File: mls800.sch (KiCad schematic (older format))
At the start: 43 parts, among them CON1 BARREL_JACK, IC1 6N137, J1 USB, P1 CONN_02X03, P2 DIN_5, P3 DIN_5, P4 CONN_02X03, P5 CONN_02X03, SW1 SW_TACT_LED, U1 LM340MP-5.0/NOPB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

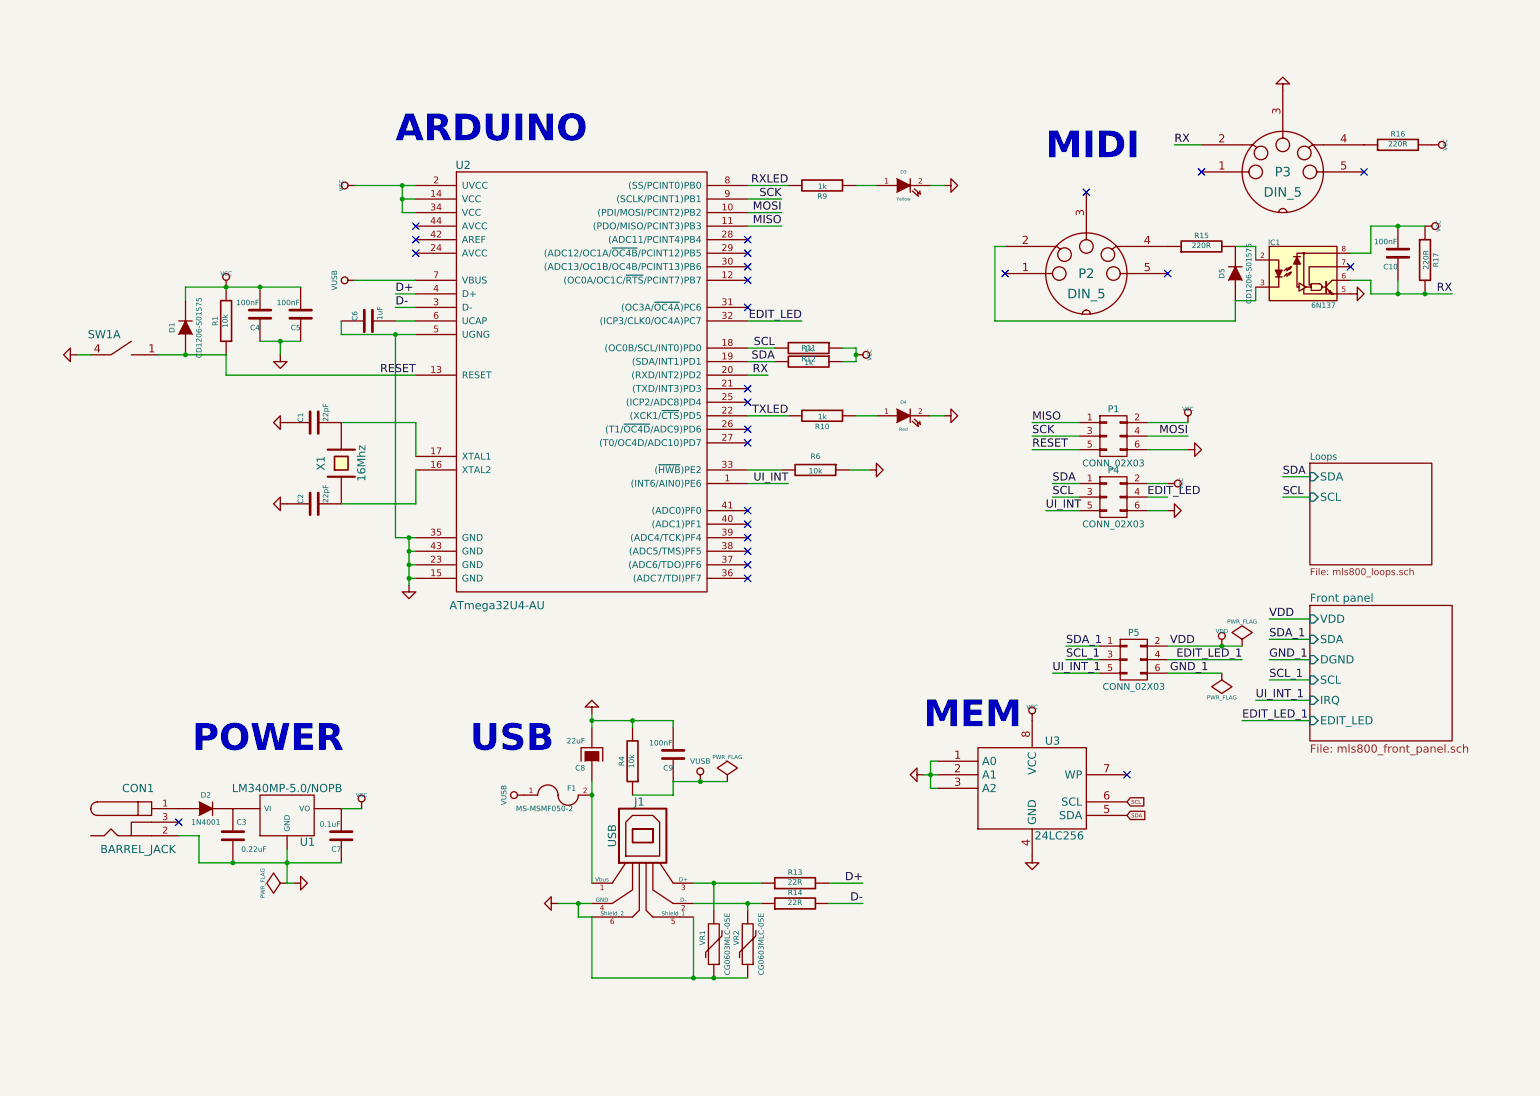
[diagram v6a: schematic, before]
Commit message: MLS800
* rerouting of some part
* added filter cap to each digital part
* added board filter cap
* set 3d shapes for remaining parts (missing custom parts)
* added footprint for small pushbutton
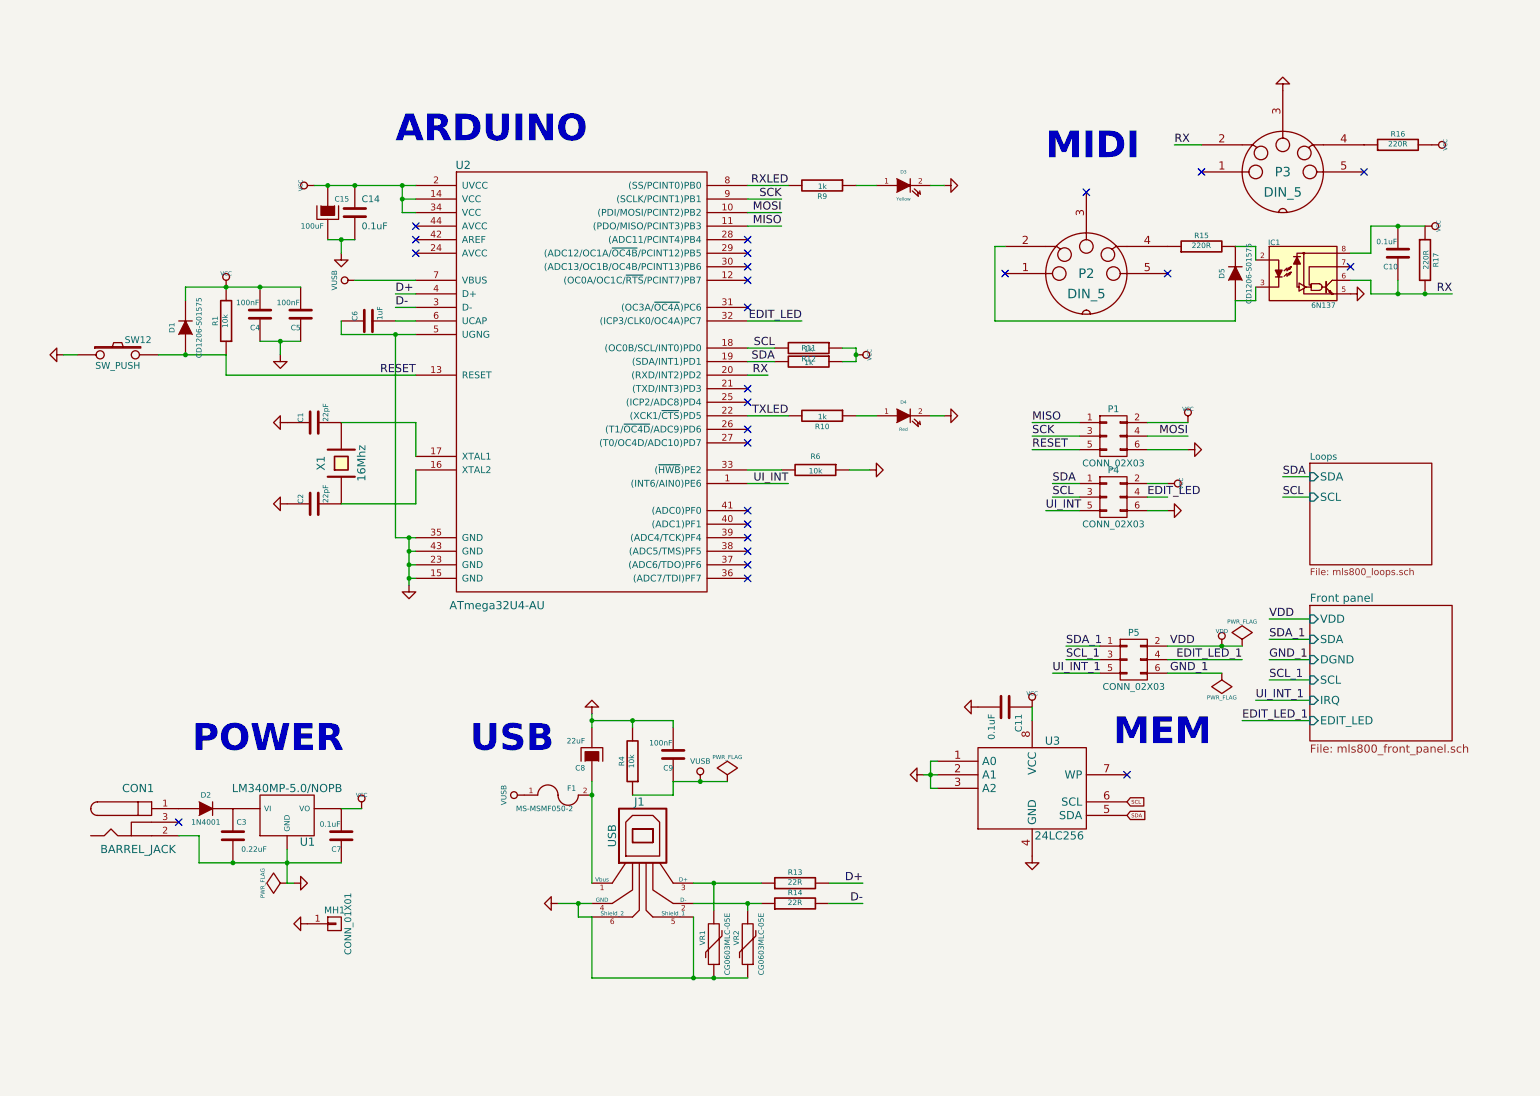
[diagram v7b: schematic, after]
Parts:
- removed SW1: SW_TACT_LED, Custom-device:MEC-5G, symbol SW_TACT_LED
- added C11, C14: 0.1uF, Capacitors_SMD:C_0805_HandSoldering, symbol C
- added C15: 100uF, Capacitors_SMD:C_0805_HandSoldering, symbol CAPAPOL
- added MH1: CONN_01X01, Connect:1pin, symbol CONN_01X01
- added SW12: SW_PUSH, Custom-device:SW_PUSH_SMALL, symbol SW_PUSH
- C10: value 100nF -> 0.1uF
- VR1, VR2: footprint SMD_Packages:SMD-0603 -> Resistors_SMD:R_0603_HandSoldering
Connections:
- net GND: now also C11.2, C14.2, C15.2, MH1.1 (P1), SW12.1
- net RESET: now also SW12.2
- net VCC: now also C11.1, C14.1, C15.1
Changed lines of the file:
@@
 $EndComp
 $Comp
-L VCOM #PWR11
+L VCOM #PWR13
 U 1 1 5350633D
 P 4100 5900
-F 0 "#PWR11" H 4100 6100 40  0001 C CNN
+F 0 "#PWR13" H 4100 6100 40  0001 C CNN
 F 1 "VUSB" H 4100 6050 40  0000 C CNN
 F 2 "" H 4100 5900 60  0000 C CNN
@@
 $EndComp
 $Comp
-L VCOM #PWR14
+L VCOM #PWR16
 U 1 1 5350654A
 P 5400 5800
-F 0 "#PWR14" H 5400 6000 40  0001 C CNN
+F 0 "#PWR16" H 5400 6000 40  0001 C CNN
 F 1 "VUSB" H 5400 5950 40  0000 C CNN
 F 2 "" H 5400 5800 60  0000 C CNN
@@
 L VCC #PWR04
 U 1 1 53A7B7A6
-P 7850 5350
-F 0 "#PWR04" H 7850 5450 30  0001 C CNN
-F 1 "VCC" H 7850 5450 30  0000 C CNN
-F 2 "" H 7850 5350 60  0000 C CNN
-F 3 "" H 7850 5350 60  0000 C CNN
-	1    7850 5350
-	1    0    0    -1
-$EndComp
-Text Notes 7050 5425 0    197  ~ 39
+P 7850 5250
+F 0 "#PWR04" H 7850 5350 30  0001 C CNN
+F 1 "VCC" H 7850 5350 30  0000 C CNN
+F 2 "" H 7850 5250 60  0000 C CNN
+F 3 "" H 7850 5250 60  0000 C CNN
+	1    7850 5250
+	1    0    0    -1
+$EndComp
+Text Notes 8450 5550 0    197  ~ 39
 MEM\n
 $Comp
@@
 F 0 "VR2" V 5810 6954 40  0000 C TNN
 F 1 "CG0603MLC-05E" V 5650 7000 40  0000 C CNN
-F 2 "SMD_Packages:SMD-0603" H 5750 7000 60  0001 C CNN
+F 2 "Resistors_SMD:R_0603_HandSoldering" H 5750 7000 60  0001 C CNN
 F 3 "" H 5750 7000 60  0000 C CNN
 	1    5750 7000
@@
 F 0 "VR1" V 5560 6954 40  0000 C TNN
 F 1 "CG0603MLC-05E" V 5400 7000 40  0000 C CNN
-F 2 "SMD_Packages:SMD-0603" H 5500 7000 60  0001 C CNN
+F 2 "Resistors_SMD:R_0603_HandSoldering" H 5500 7000 60  0001 C CNN
 F 3 "" H 5500 7000 60  0000 C CNN
 	1    5500 7000
@@
 P 10550 1900
 F 0 "C10" H 10550 2000 40  0000 L CNN
-F 1 "100nF" H 10556 1815 40  0000 L CNN
+F 1 "0.1uF" H 10556 1815 40  0000 L CNN
 F 2 "Capacitors_SMD:C_0805_HandSoldering" H 10588 1750 30  0001 C CNN
 F 3 "~" H 10550 1900 60  0000 C CNN
@@
 	1    6550 2650
 	0    1    1    0
-$EndComp
-$Comp
-L SW_TACT_LED SW1
-U 1 1 547F995D
-P 1200 2650
-F 0 "SW1" H 1000 2800 60  0000 C CNN
-F 1 "SW_TACT_LED" H 1170 2550 60  0001 C CNN
-F 2 "Custom-device:MEC-5G" H 1200 2650 60  0001 C CNN
-F 3 "" H 1200 2650 60  0000 C CNN
-	1    1200 2650
-	1    0    0    -1
 $EndComp
 $Comp
@@
 L GND #PWR016
 U 1 1 54B743C1
-P 800 2650
-F 0 "#PWR016" H 800 2650 30  0001 C CNN
-F 1 "GND" H 800 2580 30  0001 C CNN
-F 2 "" H 800 2650 60  0000 C CNN
-F 3 "" H 800 2650 60  0000 C CNN
-	1    800  2650
+P 700 2650
+F 0 "#PWR016" H 700 2650 30  0001 C CNN
+F 1 "GND" H 700 2580 30  0001 C CNN
+F 2 "" H 700 2650 60  0000 C CNN
+F 3 "" H 700 2650 60  0000 C CNN
+	1    700  2650
 	0    1    1    0
 $EndComp
@@
 L VCC #PWR025
 U 1 1 54BCB5AE
-P 2850 1400
-F 0 "#PWR025" H 2850 1500 30  0001 C CNN
-F 1 "VCC" H 2850 1500 30  0000 C CNN
-F 2 "" H 2850 1400 60  0000 C CNN
-F 3 "" H 2850 1400 60  0000 C CNN
-	1    2850 1400
+P 2550 1400
+F 0 "#PWR025" H 2550 1500 30  0001 C CNN
+F 1 "VCC" H 2550 1500 30  0000 C CNN
+F 2 "" H 2550 1400 60  0000 C CNN
+F 3 "" H 2550 1400 60  0000 C CNN
+	1    2550 1400
 	0    -1   -1   0
 $EndComp
@@
 NoConn ~ 5750 2300
 $Comp
-L VCOM #PWR8
+L VCOM #PWR10
 U 1 1 54BD4D7A
 P 2850 2100
-F 0 "#PWR8" H 2850 2300 40  0001 C CNN
+F 0 "#PWR10" H 2850 2300 40  0001 C CNN
 F 1 "VUSB" H 2850 2250 40  0000 C CNN
 F 2 "" H 2850 2100 60  0000 C CNN
@@
 	2900 6000 2750 6000
 Wire Wire Line
-	900  2650 800  2650
-Wire Wire Line
 	9600 5050 9900 5050
 Wire Wire Line
@@
 	2850 2100 3300 2100
 Wire Wire Line
-	2850 1400 3300 1400
+	2550 1400 3300 1400
 Wire Wire Line
 	3300 1600 3200 1600
@@
 $EndComp
 Connection ~ 9250 4800
+$Comp
+L SW_PUSH SW12
+U 1 1 54C5C8EB
+P 1100 2650
+F 0 "SW12" H 1250 2760 50  0000 C CNN
+F 1 "SW_PUSH" H 1100 2570 50  0000 C CNN
+F 2 "Custom-device:SW_PUSH_SMALL" H 1100 2650 60  0001 C CNN
+F 3 "" H 1100 2650 60  0000 C CNN
+	1    1100 2650
+	1    0    0    -1
+$EndComp
+$Comp
+L C C11
+U 1 1 54D9655A
+P 7650 5250
+F 0 "C11" H 7700 5350 50  0000 L CNN
+F 1 "0.1uF" H 7700 5150 50  0000 L CNN
+F 2 "Capacitors_SMD:C_0805_HandSoldering" H 7688 5100 30  0001 C CNN
+F 3 "" H 7650 5250 60  0000 C CNN
+	1    7650 5250
+	0    1    1    0
+$EndComp
+$Comp
+L GND #PWR032
+U 1 1 54D966CD
+P 7450 5250
+F 0 "#PWR032" H 7450 5250 30  0001 C CNN
+F 1 "GND" H 7450 5180 30  0001 C CNN
+F 2 "" H 7450 5250 60  0000 C CNN
+F 3 "" H 7450 5250 60  0000 C CNN
+	1    7450 5250
+	0    1    1    0
+$EndComp
+Wire Wire Line
+	7850 5350 7850 5250
+$Comp
+L C C14
+U 1 1 54DA1B0A
+P 2850 1600
+F 0 "C14" H 2900 1700 50  0000 L CNN
+F 1 "0.1uF" H 2900 1500 50  0000 L CNN
+F 2 "Capacitors_SMD:C_0805_HandSoldering" H 2888 1450 30  0001 C CNN
+F 3 "" H 2850 1600 60  0000 C CNN
+	1    2850 1600
+	1    0    0    -1
+$EndComp
+$Comp
+L GND #PWR033
+U 1 1 54DA2A03
+P 2750 1900
+F 0 "#PWR033" H 2750 1900 30  0001 C CNN
+F 1 "GND" H 2750 1830 30  0001 C CNN
+F 2 "" H 2750 1900 60  0000 C CNN
+F 3 "" H 2750 1900 60  0000 C CNN
+	1    2750 1900
+	1    0    0    -1
+$EndComp
+Wire Wire Line
+	700  2650 800  2650
+$Comp
+L CONN_01X01 MH1
+U 1 1 54D94CFD
+P 2700 6850
+F 0 "MH1" H 2700 6950 50  0000 C CNN
+F 1 "CONN_01X01" V 2800 6850 50  0000 C CNN
+F 2 "Connect:1pin" H 2700 6850 60  0001 C CNN
+F 3 "" H 2700 6850 60  0000 C CNN
+	1    2700 6850
+	1    0    0    -1
+$EndComp
+$Comp
+L GND #PWR034
+U 1 1 54D94F97
+P 2500 6850
+F 0 "#PWR034" H 2500 6850 30  0001 C CNN
+F 1 "GND" H 2500 6780 30  0001 C CNN
+F 2 "" H 2500 6850 60  0000 C CNN
+F 3 "" H 2500 6850 60  0000 C CNN
+	1    2500 6850
+	0    1    1    0
+$EndComp
+$Comp
+L CAPAPOL C15
+U 1 1 54DBFBD8
+P 2650 1600
+F 0 "C15" H 2700 1700 40  0000 L CNN
+F 1 "100uF" H 2450 1500 40  0000 L CNN
+F 2 "Capacitors_SMD:C_0805_HandSoldering" H 2750 1450 30  0001 C CNN
+F 3 "~" H 2650 1600 300 0000 C CNN
+	1    2650 1600
+	1    0    0    -1
+$EndComp
+Wire Wire Line
+	2650 1800 2850 1800
+Wire Wire Line
+	2750 1900 2750 1800
+Connection ~ 2750 1800
+Connection ~ 2850 1400
+Connection ~ 2650 1400
 $EndSCHEMATC

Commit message: MLS800
* copper zone clearance
* round drilling holes
*
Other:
- moved on the sheet: P4, P5
